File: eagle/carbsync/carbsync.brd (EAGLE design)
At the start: 100 x 63.5 mm, 30 parts, among them Q1 IRLML6344

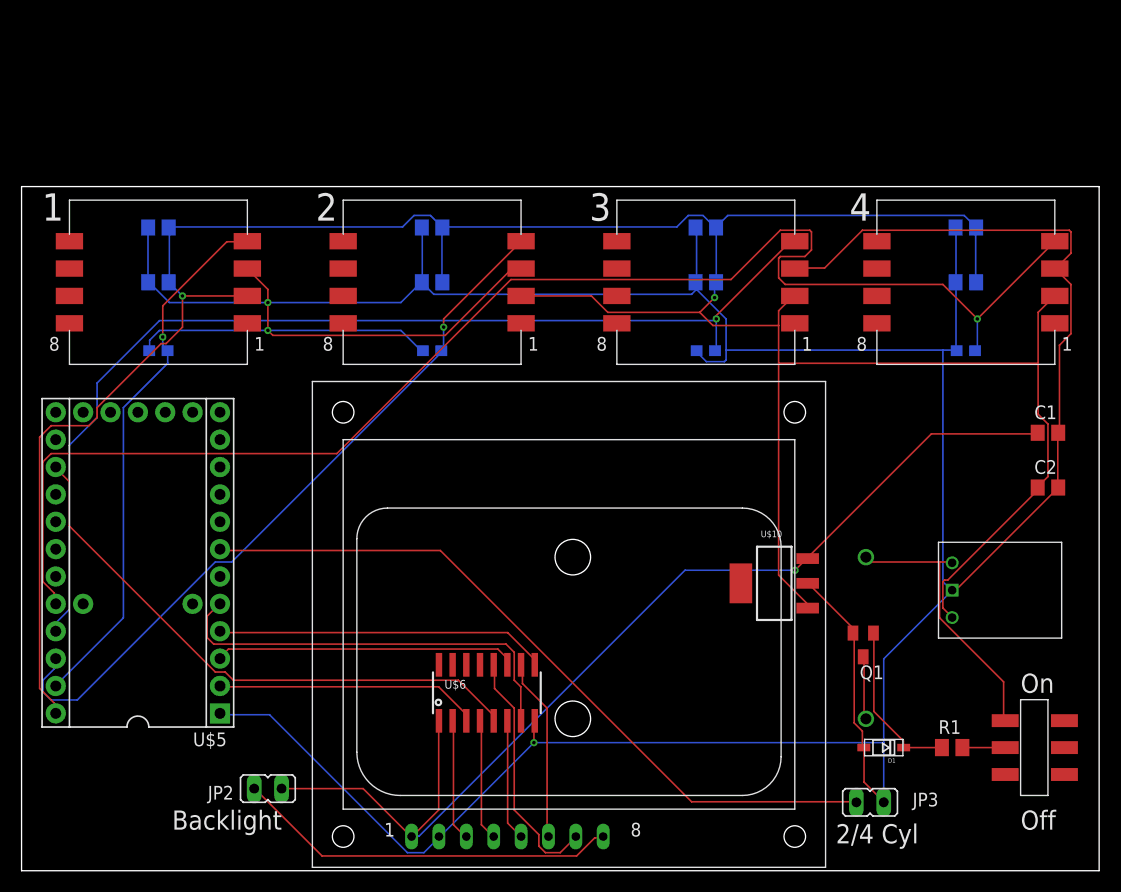
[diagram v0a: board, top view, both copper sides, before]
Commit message: update & shrink board a little
Still uses a MOSFET for reverse voltage protection,
but I'm pretty sure it won't work.
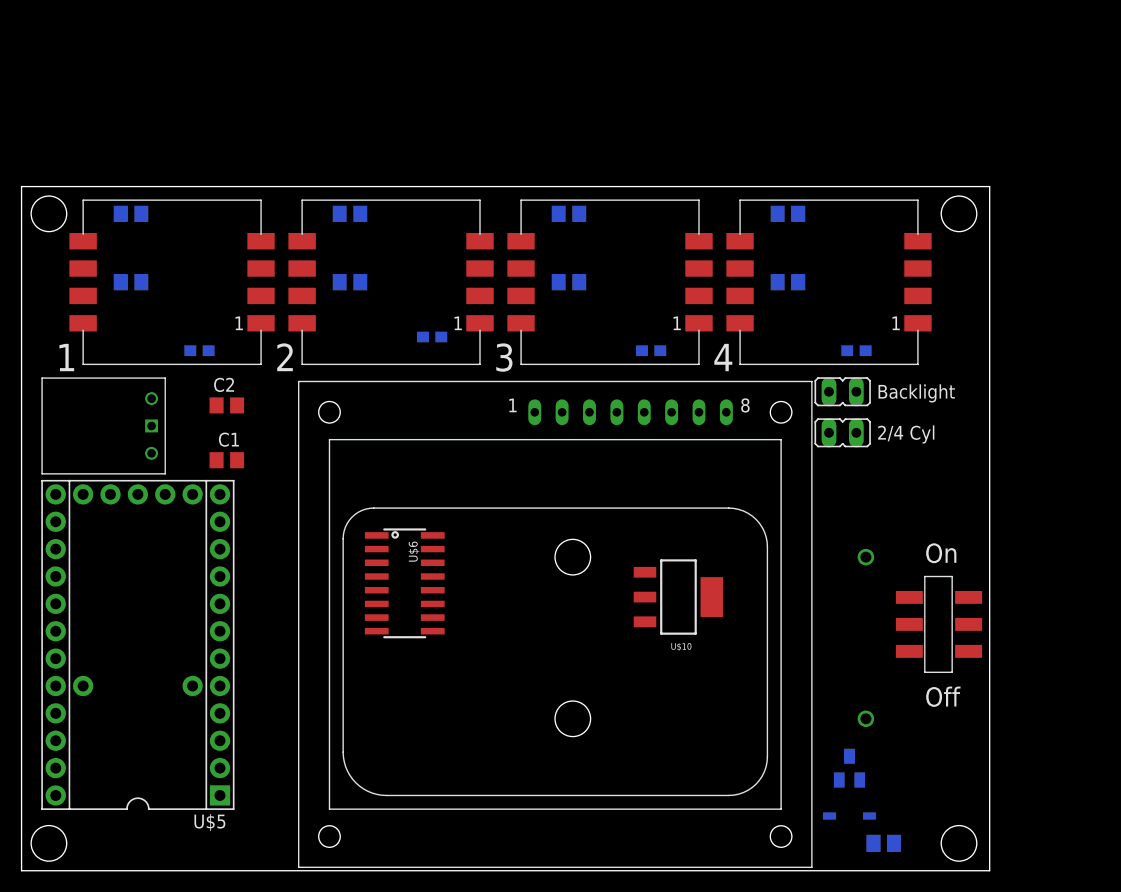
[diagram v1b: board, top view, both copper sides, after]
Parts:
- U$7: value INEX-PCD8544BPADS -> INEX-PCD8544TPINS; device synfinatic:INEX-PCD8544-BOTTOM-PADS -> synfinatic:INEX-PCD8544
- moved C2 76.6 mm to (19.1, 43.2)
- moved C1 76.2 mm to (19.1, 38.1), turned to 180 degrees
- moved U$8 72.0 mm to (13.3, 36.8), turned to 90 degrees
- moved JP2 64.8 mm to (76.2, 44.5), turned to 270 degrees
- moved JP3 34.4 mm to (76.2, 40.6)
- moved U$7 19.1 mm to (51.4, 0.64)
- moved C12 16.6 mm to (71.1, 61.0), turned to 180 degrees
- moved C13 16.5 mm to (71.1, 54.6), turned to 180 degrees
- moved S1 14.5 mm to (85.1, 22.9)
- moved C9 12.8 mm to (50.8, 61.0), turned to 180 degrees
- moved C10 12.7 mm to (50.8, 54.6), turned to 180 degrees
- moved U$6 12.7 mm to (35.6, 26.7), turned to 270 degrees
- moved U$4 12.7 mm to (74.9, 54.6)
- moved Q1 11.5 mm to (76.8, 9.53), flipped to the bottom, turned to 0 degrees
- moved R1 10.9 mm to (80.0, 2.54), flipped to the bottom, turned to 180 degrees
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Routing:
- net GND: track 382.1 -> 0.00 mm, vias 3 -> 0
- net 5V: track 272.0 -> 0.00 mm, vias 2 -> 0
- net SEN4: track 134.2 -> 0.00 mm, vias 1 -> 0
- net 3.3V: track 99.4 -> 0.00 mm, vias 1 -> 0
- net SEN3: track 97.9 -> 0.00 mm, vias 1 -> 0
- net N$10: track 68.8 -> 0.00 mm
- net SEN2: track 67.8 -> 0.00 mm, vias 1 -> 0
- net RST: track 53.1 -> 0.00 mm
- net SEN1: track 50.1 -> 0.00 mm, vias 1 -> 0
- net D/C: track 39.3 -> 0.00 mm
- net N$6: track 35.8 -> 0.00 mm
- net MOSI: track 30.8 -> 0.00 mm
- net CLK: track 28.0 -> 0.00 mm
- net VBATT: track 25.5 -> 0.00 mm
- net SCE: track 24.6 -> 0.00 mm
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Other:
- board size 100 x 63.5 mm -> 89.8 x 63.5 mm

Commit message: remove mosfet, switch to 2-DIP instead of jumpers
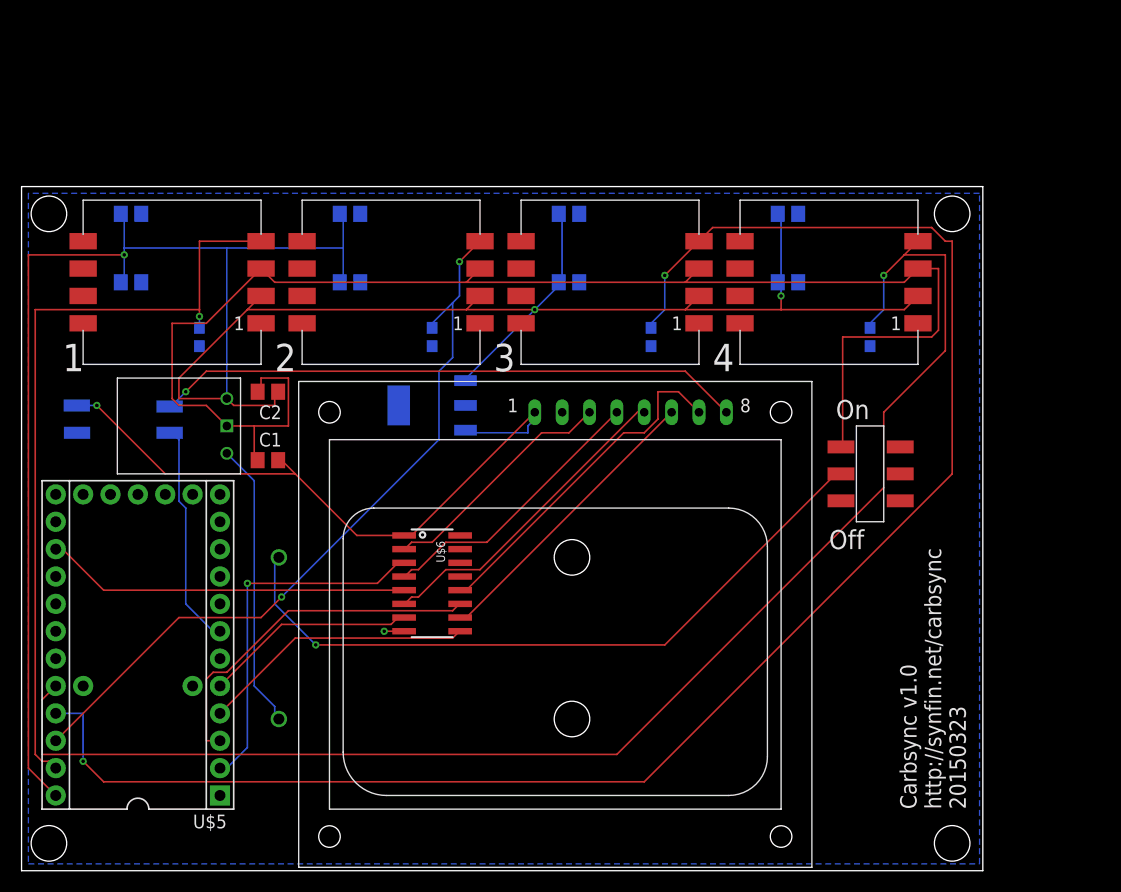
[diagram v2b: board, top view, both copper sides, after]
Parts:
- removed D1: 10V Z, adafruit:SOD-123
- removed JP2: Backlight, jumper:JP1
- removed JP3: 2/4 Cyl, jumper:JP1
- removed Q1: IRLML6344, synfinatic:SOT23
- removed R1: 13.3k, resistor:M0805
- added U$9: CT-219-X-MST, synfinatic:CT219-2-MST
- U$10: device SteelCaveRobotics-Power:SOT-223 -> synfinatic:SOT-223
- moved BAT1 68.8 mm to (81.3, 5.08), turned to 0 degrees
- moved U$10 29.0 mm to (38.1, 43.2), flipped to the bottom
- moved S1 15.3 mm to (78.7, 36.8)
- moved U$8 6.98 mm to (20.3, 36.8)
- moved C2 4.02 mm to (22.9, 44.5), turned to 180 degrees
- moved C1 3.81 mm to (22.9, 38.1)
- moved U$6 2.54 mm to (38.1, 26.7)
- moved C14 1.80 mm to (78.7, 49.5), turned to 270 degrees
- moved C11 1.27 mm to (58.4, 49.5), turned to 270 degrees
- moved C5 1.27 mm to (16.5, 49.5), turned to 270 degrees
- turned C8 to 270 degrees
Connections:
- removed net -: BAT1.GND, Q1.3
- removed net N$10: JP3.2, U$5.D0
- removed net N$6: JP2.2, U$7.P$8
- removed net N$8: D1.C, Q1.1, R1.1
- new net 4CYL: U$5.D0, U$9.P$2
- new net LED: U$7.P$8, U$9.P$4
- net 3.3V: now also U$9.P$3; no longer JP2.1
- net GND: now also S1.P$1, U$10.4, U$9.P$1; no longer D1.A, JP3.1, Q1.2
- net N$7: now also BAT1.GND; no longer R1.2
- net VBATT: no longer S1.P$1
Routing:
- net 5V: track 0.00 -> 227.5 mm, vias 0 -> 3
- net SEN3: track 0.00 -> 156.3 mm, vias 0 -> 2
- net GND: track 0.00 -> 135.8 mm, vias 0 -> 1
- net SEN4: track 0.00 -> 132.9 mm, vias 0 -> 1
- net SEN1: track 0.00 -> 72.7 mm, vias 0 -> 1
- net SEN2: track 0.00 -> 70.2 mm, vias 0 -> 2
- net N$7: track 0.00 -> 65.1 mm, vias 0 -> 1
- net 3.3V: track 0.00 -> 62.5 mm, vias 0 -> 1
- net LED: track 0.00 -> 54.6 mm, vias 0 -> 1
- net SCE: track 0.00 -> 33.9 mm, vias 0 -> 1
- net RST: track 0.00 -> 33.9 mm
- net CLK: track 0.00 -> 33.4 mm
- net N$5: track 0.00 -> 32.1 mm
- net N$3: track 0.00 -> 29.6 mm
- net N$4: track 0.00 -> 27.5 mm
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- added copper zone on layer 16, net GND
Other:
- board size 89.8 x 63.5 mm -> 89.2 x 63.5 mm
- board text added: "Carbsync v1.0 http://synfin.net/carbsync 20150323"
- board text added: "S/N:"
- board text removed: "2/4 Cyl"
- board text removed: "Backlight"

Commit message: basic 3.5x2.5" board design
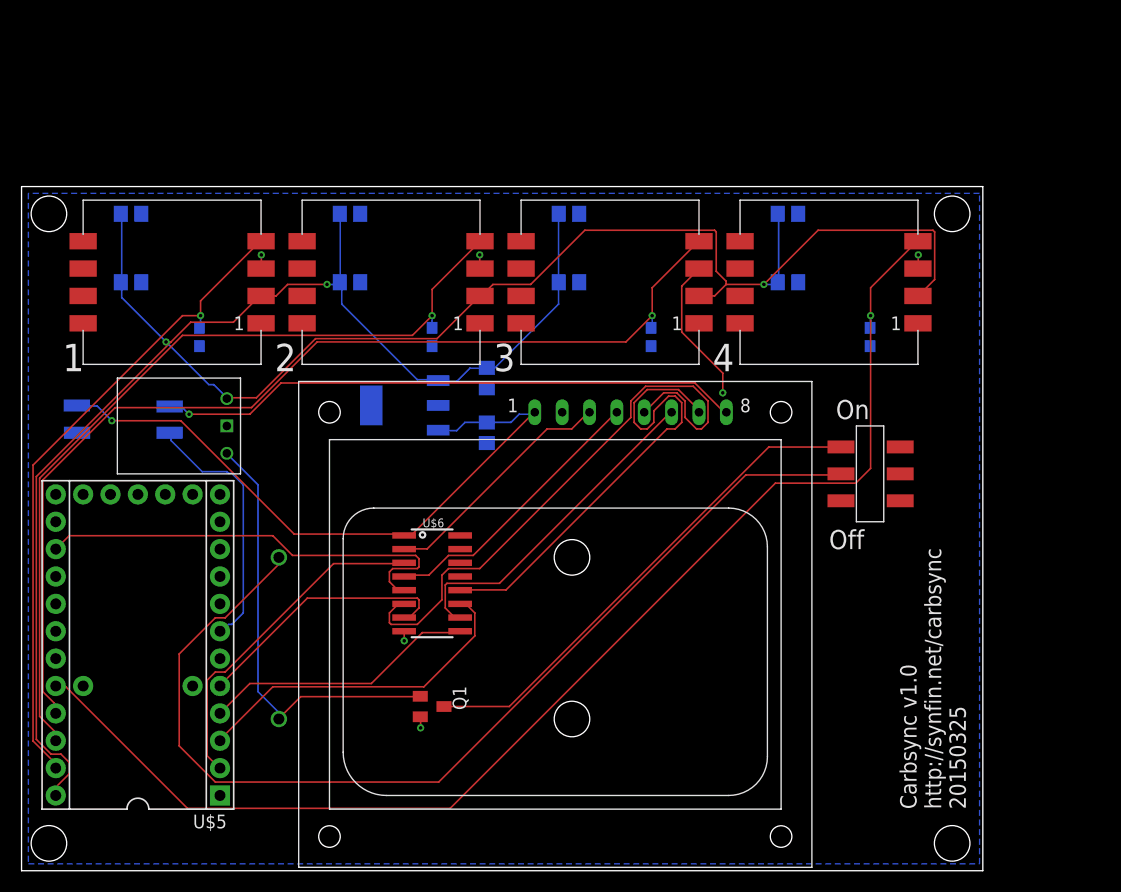
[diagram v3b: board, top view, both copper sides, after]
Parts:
- added Q1: IRLML6344, synfinatic:SOT23
- moved C1 20.5 mm to (43.2, 40.6), flipped to the bottom, turned to 270 degrees
- moved C2 20.4 mm to (43.2, 45.7), flipped to the bottom, turned to 270 degrees
- moved U$10 2.54 mm to (35.6, 43.2)
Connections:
- new net N$6: Q1.3, S1.P$1
- net GND: now also Q1.2; no longer S1.P$1
- net VBATT: now also Q1.1
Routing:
- net GND: track 135.8 -> 19.5 mm, vias 1 -> 6
- net SEN3: track 156.3 -> 95.0 mm, vias 2 -> 1
- net N$6: track 0.00 -> 46.8 mm
- net N$7: track 65.1 -> 96.5 mm, vias 1 -> 0
- net N$3: track 29.6 -> 55.4 mm
- net SEN4: track 132.9 -> 117.5 mm
- net VBATT: track 26.6 -> 40.7 mm
- net N$5: track 32.1 -> 45.0 mm
- net SEN1: track 72.7 -> 60.8 mm
- net RST: track 33.9 -> 41.4 mm
- net SEN2: track 70.2 -> 77.5 mm, vias 2 -> 1
- net D/C: track 19.7 -> 24.5 mm
- net N$4: track 27.5 -> 31.6 mm
- net 4CYL: track 20.9 -> 24.1 mm
- net SCE: track 33.9 -> 31.4 mm, vias 1 -> 0
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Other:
- board text added: "Carbsync v1.0 http://synfin.net/carbsync 20150325"
- board text removed: "Carbsync v1.0 http://synfin.net/carbsync 20150323"

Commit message: redesign PCB around http://www.hammondmfg.com/pdf/1553D_BAT.pdf
still need to find a power switch which will work correctly
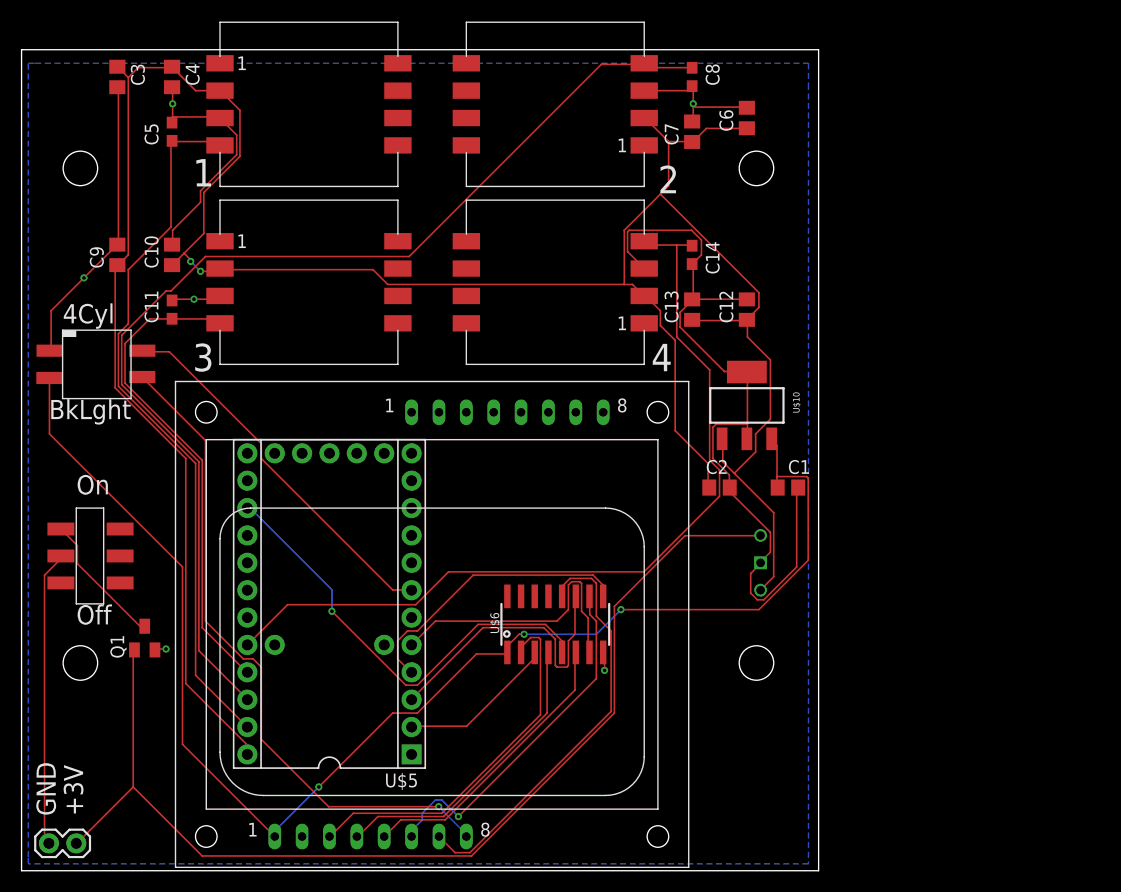
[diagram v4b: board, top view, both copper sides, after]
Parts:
- removed BAT1: 2xAA, synfinatic:BATTERY-2-AA-2462
- added JP1: M02PTH, SparkFun-Connectors:1X02
- U$7: value INEX-PCD8544TPINS -> INEX-PCD8544BOTTOM-CONNECTED; device synfinatic:INEX-PCD8544 -> synfinatic:INEX-PCD8544-TOP-BOTTOM
- moved S1 72.8 mm to (6.35, 29.2)
- moved U$8 49.7 mm to (69.8, 33.0), flipped to the bottom, turned to 270 degrees
- moved C11 44.5 mm to (14.0, 52.1), flipped to the top, turned to 90 degrees
- moved C9 42.1 mm to (8.89, 57.1), flipped to the top, turned to 90 degrees
- moved C6 37.9 mm to (67.3, 69.8), flipped to the top, turned to 90 degrees
- moved C10 36.9 mm to (14.0, 57.1), flipped to the top, turned to 90 degrees
- moved C7 34.7 mm to (62.2, 68.6), flipped to the top, turned to 90 degrees
- moved C8 34.1 mm to (62.2, 73.7), flipped to the top
- moved U$10 31.8 mm to (67.3, 43.2), flipped to the top, turned to 0 degrees
- moved C1 28.4 mm to (71.1, 35.6), flipped to the top, turned to 0 degrees
- moved U$3 27.9 mm to (26.7, 54.6), turned to 180 degrees
- moved Q1 27.4 mm to (11.4, 21.6), turned to 0 degrees
- moved U$4 25.4 mm to (49.5, 54.6)
- moved C2 23.9 mm to (64.8, 35.6), flipped to the top, turned to 0 degrees
- moved U$7 22.9 mm to (38.7, 19.7)
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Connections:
- removed net N$7: BAT1.GND, S1.P$2
- new net VGND: JP1.2, S1.P$2
- net VBATT: now also JP1.1; no longer BAT1.+3V
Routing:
- net GND: track 19.5 -> 145.6 mm
- net N$7: track 96.5 -> 0.00 mm
- net 3.3V: track 62.0 -> 127.4 mm, vias 1 -> 3
- net VBATT: track 40.7 -> 99.2 mm
- net SEN3: track 95.0 -> 45.2 mm, vias 1 -> 0
- net SEN4: track 117.5 -> 79.1 mm, vias 1 -> 0
- net N$6: track 46.8 -> 12.5 mm
- net N$3: track 55.4 -> 26.8 mm
- net VGND: track 0.00 -> 27.5 mm
- net SEN2: track 77.5 -> 102.2 mm, vias 1 -> 0
- net SCE: track 31.4 -> 14.6 mm
- net 5V: track 228.7 -> 244.3 mm, vias 3 -> 2
- net N$1: track 22.5 -> 34.1 mm
- net 4CYL: track 24.1 -> 35.0 mm
- net LED: track 54.3 -> 61.7 mm
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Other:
- board size 89.2 x 63.5 mm -> 74 x 76.2 mm
- board text added: "+3V"
- board text added: "4Cyl"
- board text added: "BkLght"
- board text added: "GND"
- board text removed: "Carbsync v1.0 http://synfin.net/carbsync 20150325"
- board text removed: "S/N:"

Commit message: clean up board and fix the level shifter
Waiting on part order to check footprints & do power switch
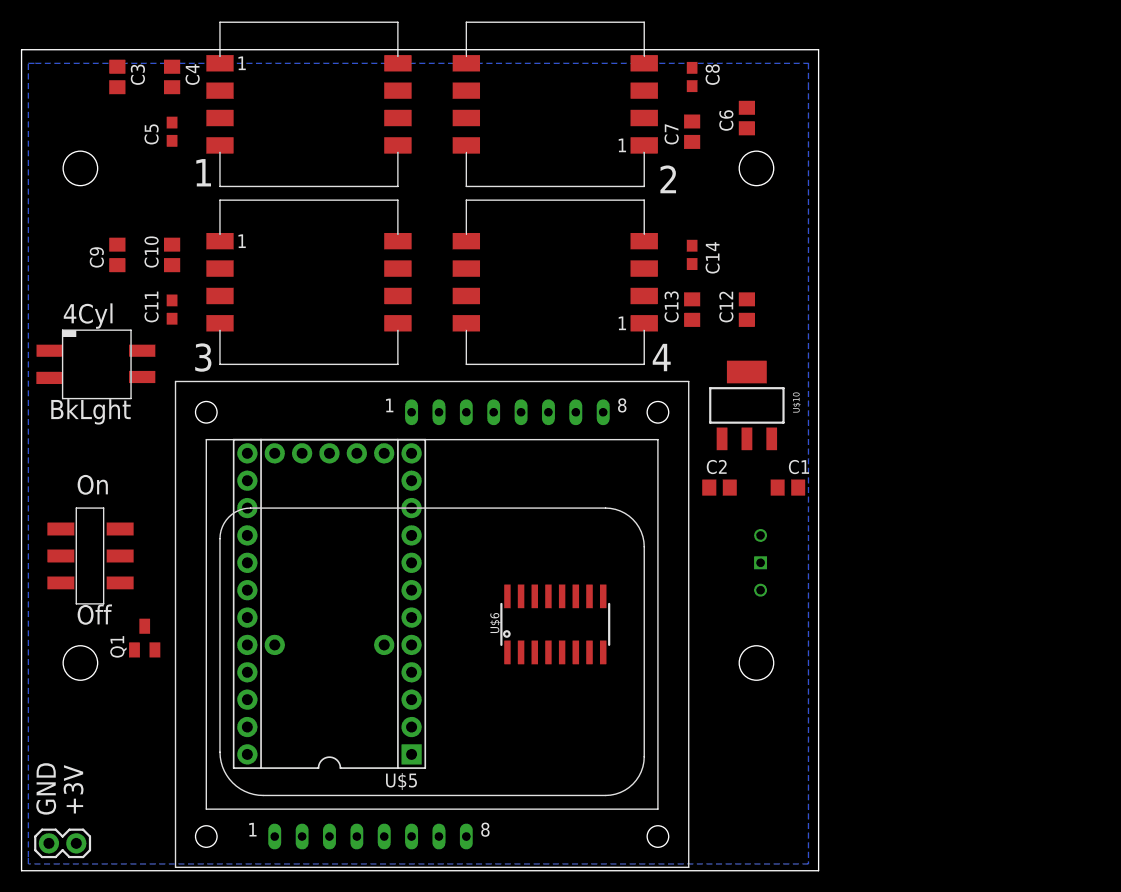
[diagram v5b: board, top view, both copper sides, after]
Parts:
- U$6: value 74HC4050D -> HEF4050BT
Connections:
- net GND: now also U$6.14
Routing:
- net 5V: track 244.3 -> 0.00 mm, vias 2 -> 0
- net GND: track 145.6 -> 0.00 mm, vias 6 -> 0
- net 3.3V: track 127.4 -> 0.00 mm, vias 3 -> 0
- net SEN2: track 102.2 -> 0.00 mm
- net VBATT: track 99.2 -> 0.00 mm
- net SEN4: track 79.1 -> 0.00 mm
- net SEN1: track 66.0 -> 0.00 mm
- net LED: track 61.7 -> 0.00 mm, vias 1 -> 0
- net SEN3: track 45.2 -> 0.00 mm
- net RST: track 41.2 -> 0.00 mm, vias 1 -> 0
- net N$5: track 39.1 -> 0.00 mm
- net 4CYL: track 35.0 -> 0.00 mm
- net N$1: track 34.1 -> 0.00 mm
- net N$4: track 33.1 -> 0.00 mm, vias 1 -> 0
- net N$2: track 28.1 -> 0.00 mm
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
